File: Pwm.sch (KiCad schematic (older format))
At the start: 15 parts, among them P2 CONN_01X03, P3 CONN_01X03, P4 CONN_01X03, P5 CONN_01X03, U9 PCA9551

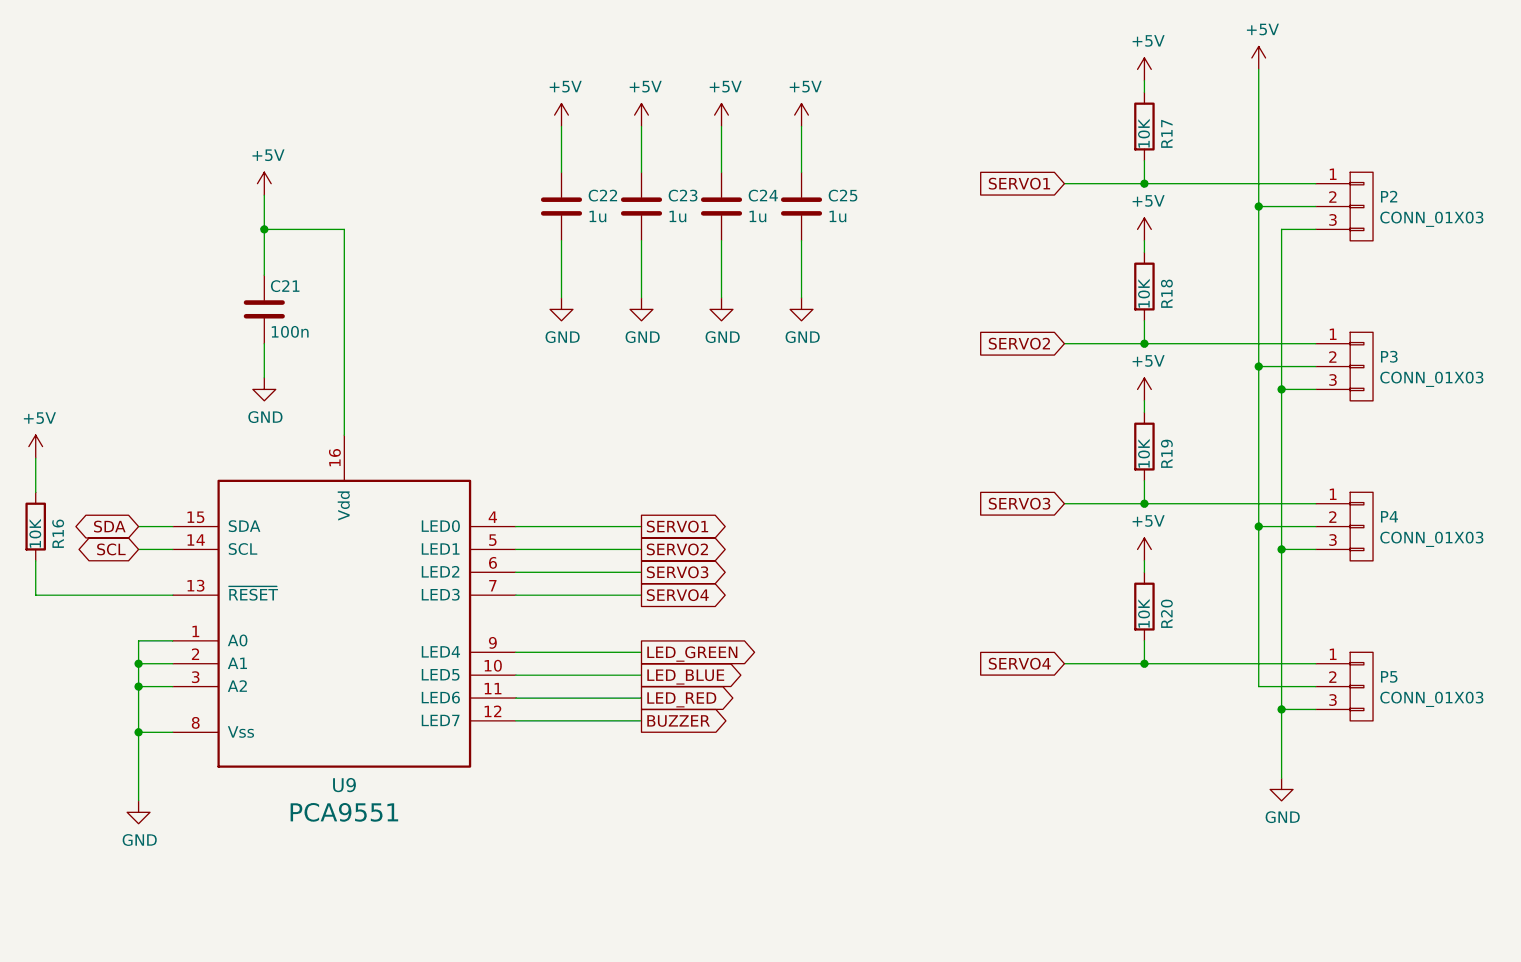
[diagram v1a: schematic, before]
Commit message: cambiado el driver led al PCA9634
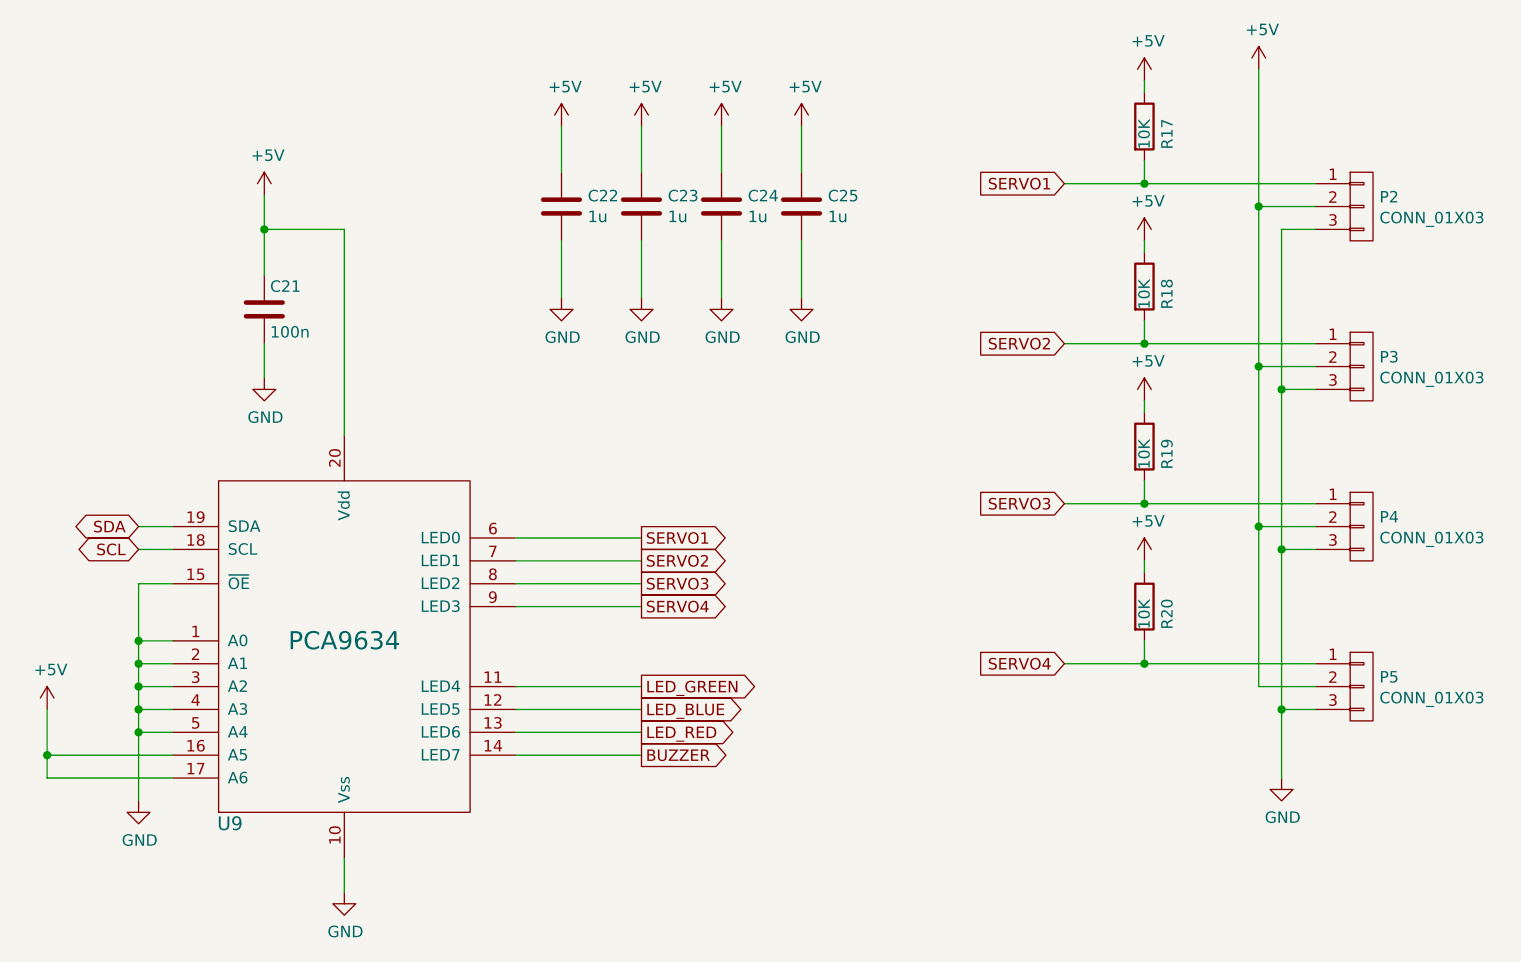
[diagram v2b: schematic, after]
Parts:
- removed R16: 10K, Resistencias:R_0805, symbol R
- removed U9: PCA9551, Housings_SSOP:TSSOP-16_4.4x5mm_Pitch0.65mm, symbol PCA9551
- added U9: PCA9634, Housings_SSOP:TSSOP-20_4.4x6.5mm_Pitch0.65mm, symbol PCA9634
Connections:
- net +5V: now also U9.16 (A5), U9.17 (A6), U9.20 (Vdd)
- net BUZZER: now also U9.14 (LED7)
- net GND: now also U9.1 (A0), U9.10 (Vss), U9.15 (~OE), U9.2 (A1), U9.3 (A2), U9.4 (A3), U9.5 (A4)
- net LED_BLUE: now also U9.12 (LED5)
- net LED_GREEN: now also U9.11 (LED4)
- net LED_RED: now also U9.13 (LED6)
- net SCL: now also U9.18 (SCL)
- net SDA: now also U9.19 (SDA)
- net SERVO1: now also U9.6 (LED0)
- net SERVO2: now also U9.7 (LED1)
- net SERVO3: now also U9.8 (LED2)
- net SERVO4: now also U9.9 (LED3)
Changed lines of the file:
@@
 EESchema Schematic File Version 2
+LIBS:Wifi_PB-rescue
 LIBS:power
 LIBS:device
@@
 $EndBitmap
 $Comp
-L PCA9551 U9
-U 1 1 586D5351
-P 1550 3800
-F 0 "U9" H 2100 3717 60  0000 C CNN
-F 1 "PCA9551" H 2100 3597 79  0000 C CNN
-F 2 "Housings_SSOP:TSSOP-16_4.4x5mm_Pitch0.65mm" H 1550 3930 60  0001 C CNN
-F 3 "" H 1550 3930 60  0001 C CNN
-F 4 "510-730" H 2300 3600 60  0001 C CNN "Ref_Proveedor"
-F 5 "nxp" H 1950 3700 60  0001 C CNN "Fabricante"
-F 6 "PCA9551PW" H 2350 3700 60  0001 C CNN "Ref"
-F 7 "rs" H 2000 3600 60  0001 C CNN "Provedor"
-F 8 "" H 1550 3800 60  0001 C CNN "Tolerancia"
-F 9 "" H 1550 3800 60  0001 C CNN "Potencia"
-	1    1550 3800
-	1    0    0    -1
-$EndComp
-$Comp
 L CONN_01X03 P4
 U 1 1 586D53FE
@@
 	1750 2100 1750 1950
 Wire Wire Line
-	2850 2750 3400 2750
+	2850 2800 3400 2800
 Wire Wire Line
-	2850 2850 3400 2850
+	2850 2900 3400 2900
 Wire Wire Line
-	2850 2950 3400 2950
+	2850 3000 3400 3000
 Wire Wire Line
-	2850 3050 3400 3050
+	2850 3100 3400 3100
 Wire Wire Line
-	2850 3300 3400 3300
+	2850 3450 3400 3450
 Wire Wire Line
-	2850 3400 3400 3400
+	2850 3550 3400 3550
 Wire Wire Line
-	2850 3500 3400 3500
+	2850 3650 3400 3650
 Wire Wire Line
-	2850 3600 3400 3600
+	2850 3750 3400 3750
 Wire Wire Line
 	1200 3650 1350 3650
 Wire Wire Line
-	1200 3250 1200 3950
+	1200 3000 1200 3950
 $Comp
 L GND #PWR082
@@
 Text GLabel 1200 2850 0    50   BiDi ~ 0
 SCL
-Text GLabel 3400 3500 2    50   Output ~ 0
+Text GLabel 3400 3650 2    50   Output ~ 0
 LED_RED
-Text GLabel 3400 3300 2    50   Output ~ 0
+Text GLabel 3400 3450 2    50   Output ~ 0
 LED_GREEN
-Text GLabel 3400 3400 2    50   Output ~ 0
+Text GLabel 3400 3550 2    50   Output ~ 0
 LED_BLUE
-Text GLabel 3400 3600 2    50   Output ~ 0
+Text GLabel 3400 3750 2    50   Output ~ 0
 BUZZER
-Text GLabel 3400 2750 2    50   Output ~ 0
+Text GLabel 3400 2800 2    50   Output ~ 0
 SERVO1
-Text GLabel 3400 2850 2    50   Output ~ 0
+Text GLabel 3400 2900 2    50   Output ~ 0
 SERVO2
-Text GLabel 3400 2950 2    50   Output ~ 0
+Text GLabel 3400 3000 2    50   Output ~ 0
 SERVO3
-Text GLabel 3400 3050 2    50   Output ~ 0
+Text GLabel 3400 3100 2    50   Output ~ 0
 SERVO4
 Text GLabel 5250 1250 0    50   Input ~ 0
@@
 Wire Wire Line
 	5600 2250 5600 2200
-Wire Wire Line
-	750  2900 750  3050
-Wire Wire Line
-	750  3050 1350 3050
-$Comp
-L +5V #PWR088
-U 1 1 58700007
-P 750 2450
-F 0 "#PWR088" H 750 2300 50  0001 C CNN
-F 1 "+5V" H 765 2623 50  0000 C CNN
-F 2 "" H 750 2450 50  0000 C CNN
-F 3 "" H 750 2450 50  0000 C CNN
-	1    750  2450
-	1    0    0    -1
-$EndComp
-Wire Wire Line
-	750  2450 750  2600
-$Comp
-L R R16
-U 1 1 58700C10
-P 750 2750
-F 0 "R16" V 850 2650 50  0000 L CNN
-F 1 "10K" V 750 2650 50  0000 L CNN
-F 2 "Resistencias:R_0805" V 680 2750 50  0001 C CNN
-F 3 "" H 750 2750 50  0000 C CNN
-F 4 "VISHAY" H 750 2750 60  0001 C CNN "Fabricante"
-F 5 "CRCW080510K0FKEA" H 750 2750 60  0001 C CNN "Ref"
-F 6 "1/8W" H 750 2750 60  0001 C CNN "Potencia"
-F 7 "1%" H 750 2750 60  0001 C CNN "Tolerancia"
-F 8 "TME" H 750 2750 60  0001 C CNN "Provedor"
-F 9 "CRCW080510K0FKEA" H 750 2750 60  0001 C CNN "Ref_Proveedor"
-	1    750  2750
-	1    0    0    -1
-$EndComp
 $Comp
 L R R20
@@
 EndData
 $EndBitmap
+$Comp
+L PCA9634 U9
+U 1 1 58C5CF56
+P 1550 4000
+F 0 "U9" H 1600 3950 60  0000 C CNN
+F 1 "PCA9634" H 2100 4750 79  0000 C CNN
+F 2 "Housings_SSOP:TSSOP-20_4.4x6.5mm_Pitch0.65mm" H -600 1330 60  0001 C CNN
+F 3 "" H -600 1330 60  0001 C CNN
+F 4 "~" H 1550 4000 60  0001 C CNN "Fabricante"
+F 5 "~" H 1550 4000 60  0001 C CNN "Ref"
+F 6 "~" H 1550 4000 60  0001 C CNN "Potencia"
+F 7 "~" H 1550 4000 60  0001 C CNN "Tolerancia"
+F 8 "~" H 1550 4000 60  0001 C CNN "Provedor"
+F 9 "~" H 1550 4000 60  0001 C CNN "Ref_Proveedor"
+F 10 "~" H 1550 4000 60  0001 C CNN "Provider_2"
+F 11 "~" H 1550 4000 60  0001 C CNN "Ref_Provider_2"
+	1    1550 4000
+	1    0    0    -1
+$EndComp
+$Comp
+L GND #PWR088
+U 1 1 58C5D109
+P 2100 4350
+F 0 "#PWR088" H 2100 4100 50  0001 C CNN
+F 1 "GND" H 2105 4177 50  0000 C CNN
+F 2 "" H 2100 4350 50  0000 C CNN
+F 3 "" H 2100 4350 50  0000 C CNN
+	1    2100 4350
+	1    0    0    -1
+$EndComp
+Wire Wire Line
+	2100 4350 2100 4200
+$Comp
+L +5V #PWR089
+U 1 1 58C5D20D
+P 800 3550
+F 0 "#PWR089" H -100 -300 50  0001 C CNN
+F 1 "+5V" H 815 3723 50  0000 C CNN
+F 2 "" H -100 -150 50  0001 C CNN
+F 3 "" H -100 -150 50  0001 C CNN
+	1    800  3550
+	1    0    0    -1
+$EndComp
+Wire Wire Line
+	800  3550 800  3850
+Wire Wire Line
+	800  3850 1350 3850
+Wire Wire Line
+	1350 3750 800  3750
+Connection ~ 800  3750
+Wire Wire Line
+	1200 3550 1350 3550
+Connection ~ 1200 3550
+Wire Wire Line
+	1200 3000 1350 3000
+Connection ~ 1200 3250
 $EndSCHEMATC
